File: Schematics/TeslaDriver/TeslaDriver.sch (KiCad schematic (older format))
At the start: 53 parts, among them P1 CONTROL, P2 PWR_IN+, P3 PWR_GND, P4 PWR_OUT_L2, P5 PWR_OUT_L1, Q1 STP65NF06, Q2 STP65NF06, Q3 STP65NF06, Q4 STP65NF06, T1 GateTR10x4, T2 GateTR10x4, T3 GateTR10x4, T4 GateTR10x4, U1 DS18B20, U2 DS18B20, U3 UCC27424D, U4 UCC27424D

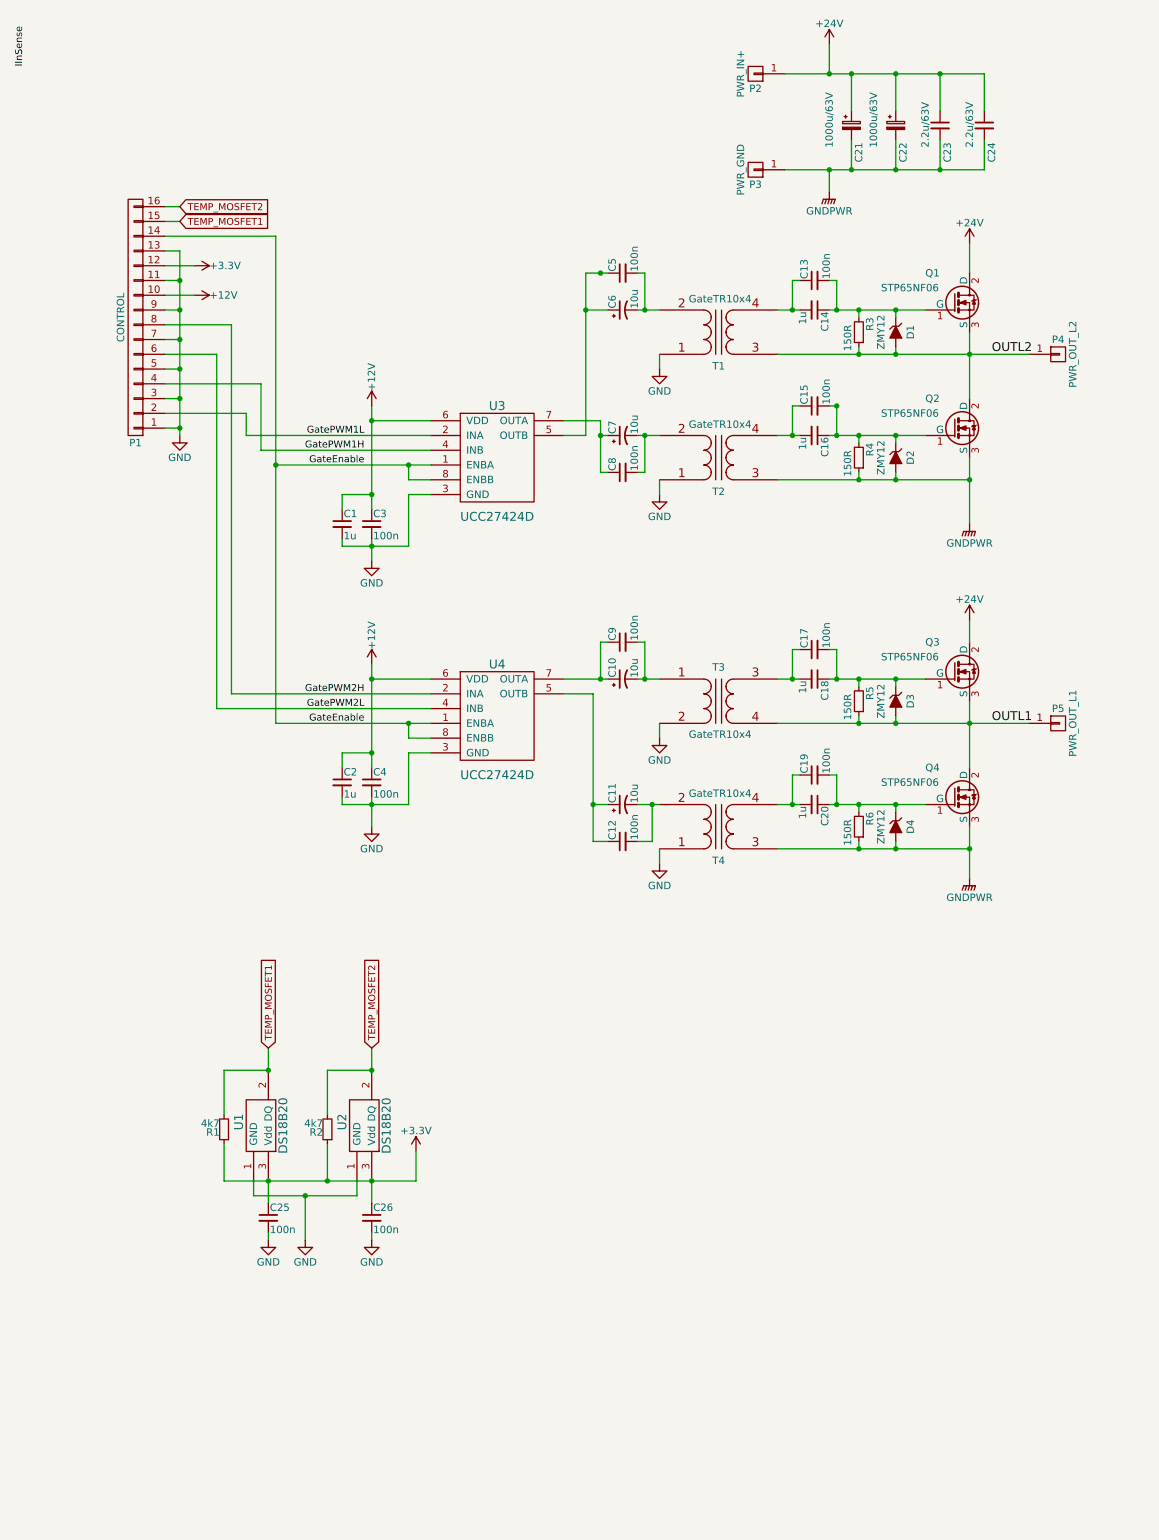
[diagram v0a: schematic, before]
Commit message: * Redesigned the inverter gate driver. 	- It will now drive the gate to ~+-12V rather than ~-0.6 to 11.4. 	- Redesigned the gate clamping to better enforce the gate voltage 	  limit and to more quickly adapt the gate transformers DC level when 	  changing duty cycle.
* Redesigned the inverter PCB.
	- Made an entirely new layout for the inverter PCB which hopefully
	  will be able to carry substantial currents without needing extra
	  bus bars. It should also give parasitic inductances on the board
	  less oportunity to mess with the GS voltage.
	- Designed for manufacturing on a board-hose rather than home
	  etch.
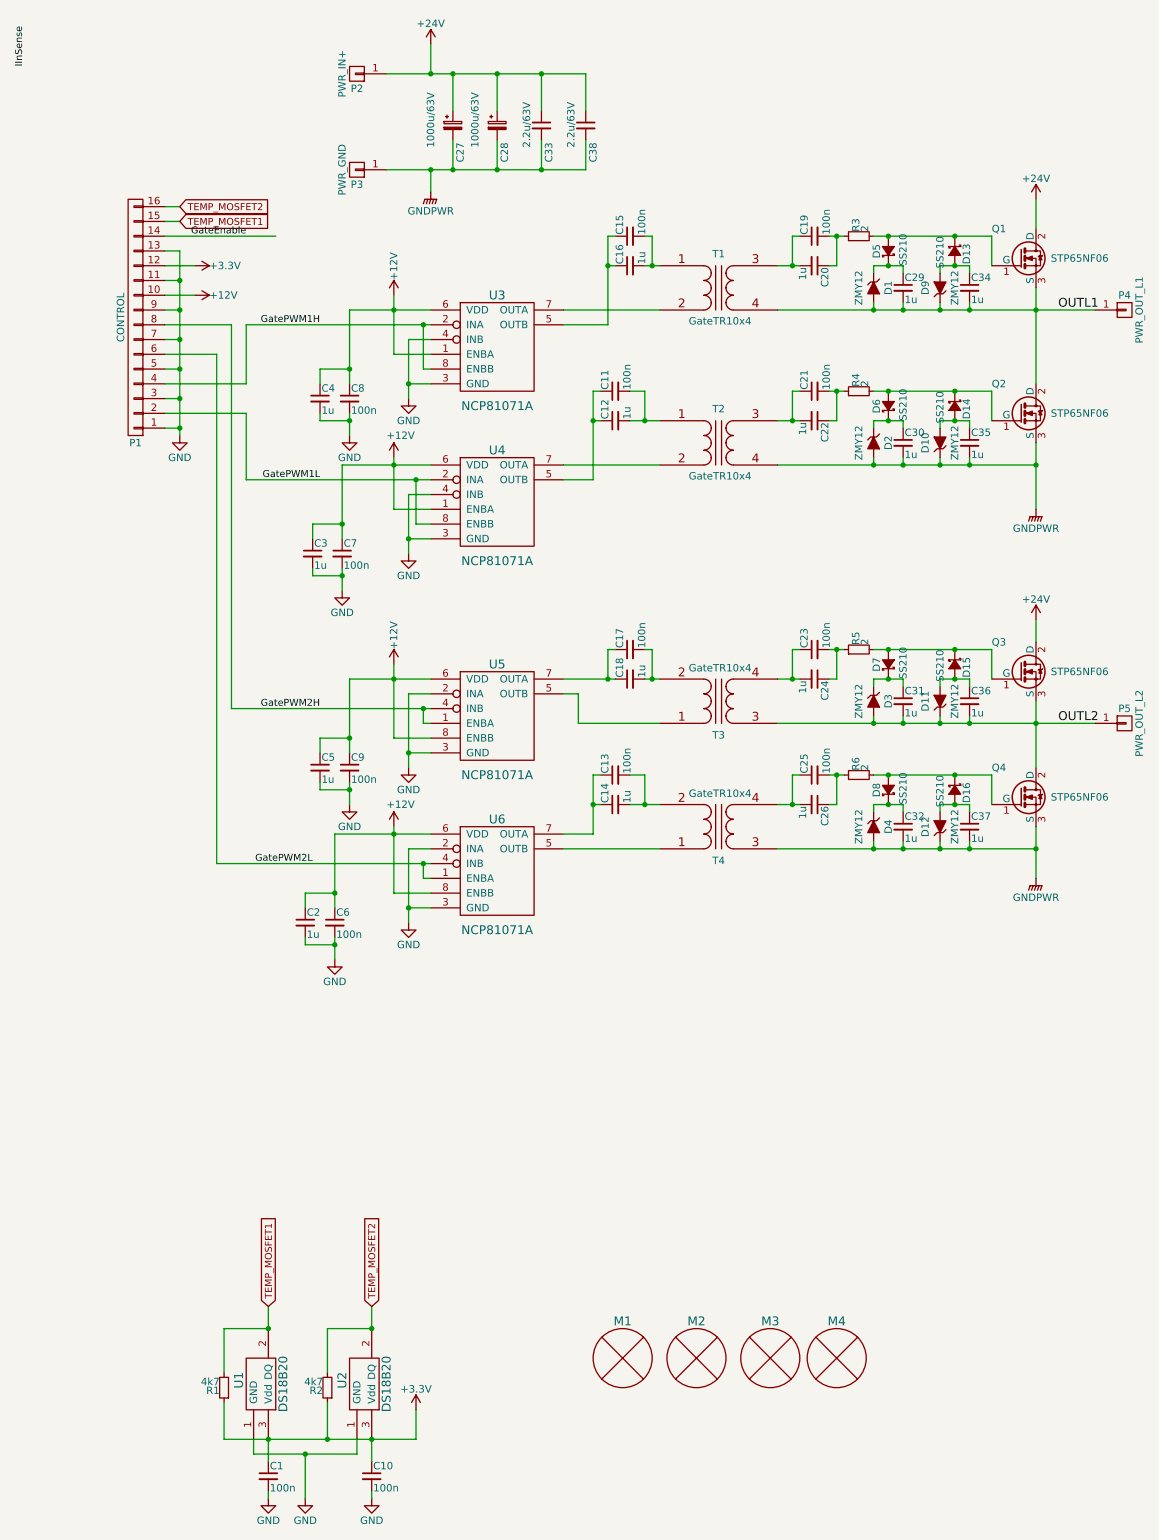
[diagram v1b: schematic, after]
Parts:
- removed C10, C11, C6, C7: 10u, Capacitors_Tantalum_SMD:TantalC_SizeB_EIA-3528_Reflow, symbol CP1_Small
- removed C15, C4, C8: 100n, MyCapacitors:C_0603, symbol C_Small
- removed U3, U4: UCC27424D, MyFootprints:SOIC-8_3.9x4.9mm_Pitch1.27mm, symbol UCC27424D
- added C11, C21, C23, C25, C6, C7: 100n, MyCapacitors:C_0603, symbol C_Small
- added C22, C24, C26: 1u, Capacitors_SMD:C_0603, symbol C_Small
- added C29, C3, C30, C31, C32, C34, C35, C36, C37, C5: 1u, MyCapacitors:C_0603, symbol C_Small
- added D10, D11, D12, D9: ZMY12, MyDiodes:MELF_Standard, symbol ZENERsmall
- added D13, D14, D15, D16, D5, D6, D7, D8: SS210, MyDiodes:Diode-SMA_Standard, symbol SS210
- added M1, M2, M3, M4: MountingHole, MyMechanical:MH7x3, symbol MountingHole
- added U3, U4, U5, U6: NCP81071A, MyFootprints:SOIC-8_3.9x4.9mm_Pitch1.27mm, symbol NCP81071A
- C12: value 100n -> 1u
- C14, C16, C18: footprint Capacitors_SMD:C_0603 -> MyCapacitors:C_0603
- P2, P3: footprint MyConnectors:PowerPad10 -> MyConnectors:PowerPad15_5
- P4: value PWR_OUT_L2 -> PWR_OUT_L1; footprint MyConnectors:PowerPad10 -> MyConnectors:PowerPad15_5
- P5: value PWR_OUT_L1 -> PWR_OUT_L2; footprint MyConnectors:PowerPad10 -> MyConnectors:PowerPad15_5
- R3, R4, R5, R6: value 150R -> 2
- renumbered C25 to C1, C26 to C10, C5 to C15, C21 to C27, C22 to C28, C23 to C33, C24 to C38, C1 to C4, C3 to C8
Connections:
- net +12V: now also C9.1, C3.1, C5.1, C6.1, C7.1, U3.1 (ENBA), U3.6 (VDD), U4.1 (ENBA), U4.6 (VDD), U5.6 (VDD), U5.8 (ENBB), U6.6 (VDD), U6.8 (ENBB)
- net GND: now also C9.2, C3.2, C5.2, C6.2, C7.2, U3.3 (GND), U3.4 (INB), U4.3 (GND), U4.4 (INB), U5.2 (INA), U5.3 (GND), U6.2 (INA), U6.3 (GND); no longer T1.1 (P1), T2.1 (P1), T3.2 (P2), T4.1 (P1)
- net GNDPWR: now also T2.4 (S2), C30.2, C32.2, C35.2, C37.2, D10.1 (K), D12.1 (K); no longer R4.1, R6.1, T2.3 (S1)
- net GatePWM1H: now also U3.2 (INA), U3.8 (ENBB)
- net GatePWM1L: now also U4.2 (INA), U4.8 (ENBB)
- net GatePWM2H: now also U5.1 (ENBA), U5.4 (INB)
- net GatePWM2L: now also U6.1 (ENBA), U6.4 (INB)
- net OUTL1: now also D1.2 (A), P4.1 (P1), Q1.3 (S), Q2.2 (D), T1.4 (S2), C29.2, C34.2, D9.1 (K); no longer D3.2 (A), P5.1 (P1), Q3.3 (S), Q4.2 (D), R5.1, T3.4 (S2)
- net OUTL2: now also D3.2 (A), P5.1 (P1), Q3.3 (S), Q4.2 (D), T3.3 (S1), C31.2, C36.2, D11.1 (K); no longer D1.2 (A), P4.1 (P1), Q1.3 (S), Q2.2 (D), R3.1, T1.3 (S1)
- net at C15.1: now also C16.1, U3.5 (OUTB)
- net at C15.2: now also C16.2, T1.1 (P1); no longer T1.2 (P2)
- net at Q2.1 (G), R4.2: now also D14.1 (K), D6.2 (A); no longer C16.1, D2.1 (K)
- net at T2.2 (P2): now also U4.7 (OUTA)
- net at C12.1: now also C11.1, U4.5 (OUTB)
- net at T3.1 (P1): now also U5.5 (OUTB); no longer C9.2
- net at C12.2: now also T2.1 (P1), C11.2; no longer T4.2 (P2)
- net at C19.1, C20.2: now also T1.3 (S1); no longer T4.4 (S2)
- new net: D13.1 (K), D5.2 (A), Q1.1 (G), R3.2
- new net: T1.2 (P2), U3.7 (OUTA)
- new net: C21.1, C22.2, T2.3 (S1)
- new net: D15.1 (K), D7.2 (A), Q3.1 (G), R5.2
- new net: C17.2, C18.2, T3.2 (P2)
- new net: C23.1, C24.2, T3.4 (S2)
- new net: D16.1 (K), D8.2 (A), Q4.1 (G), R6.2
- new net: T4.1 (P1), U6.5 (OUTB)
- new net: C13.2, C14.2, T4.2 (P2)
- new net: C25.1, C26.2, T4.4 (S2)
- new net: C17.1, C18.1, U5.7 (OUTA)
- new net: C13.1, C14.1, U6.7 (OUTA)
- new net: C32.1, D4.1 (K), D8.1 (K)
- new net: C37.1, D12.2 (A), D16.2 (A)
- new net: C25.2, C26.1, R6.1
- new net: C31.1, D3.1 (K), D7.1 (K)
- new net: C36.1, D11.2 (A), D15.2 (A)
- new net: C23.2, C24.1, R5.1
- new net: C30.1, D2.1 (K), D6.1 (K)
- new net: C35.1, D10.2 (A), D14.2 (A)
- new net: C21.2, C22.1, R4.1
- new net: C29.1, D1.1 (K), D5.1 (K)
- new net: C34.1, D13.2 (A), D9.2 (A)
- new net: C19.2, C20.1, R3.1
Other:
- moved on the sheet: C1, C10, C15, C27, C28, C33, C38, C4, C8, P2, P3, P4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

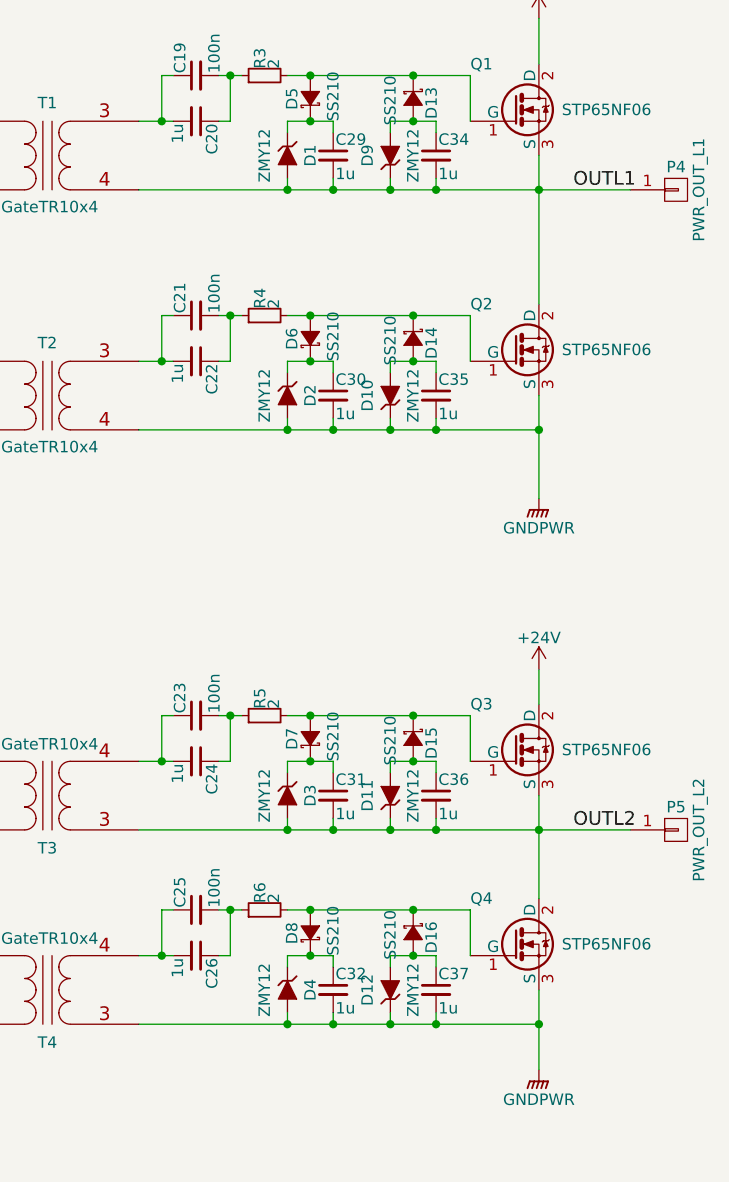
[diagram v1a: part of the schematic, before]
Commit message: Did some small component value tweeks and sorted the BOM.
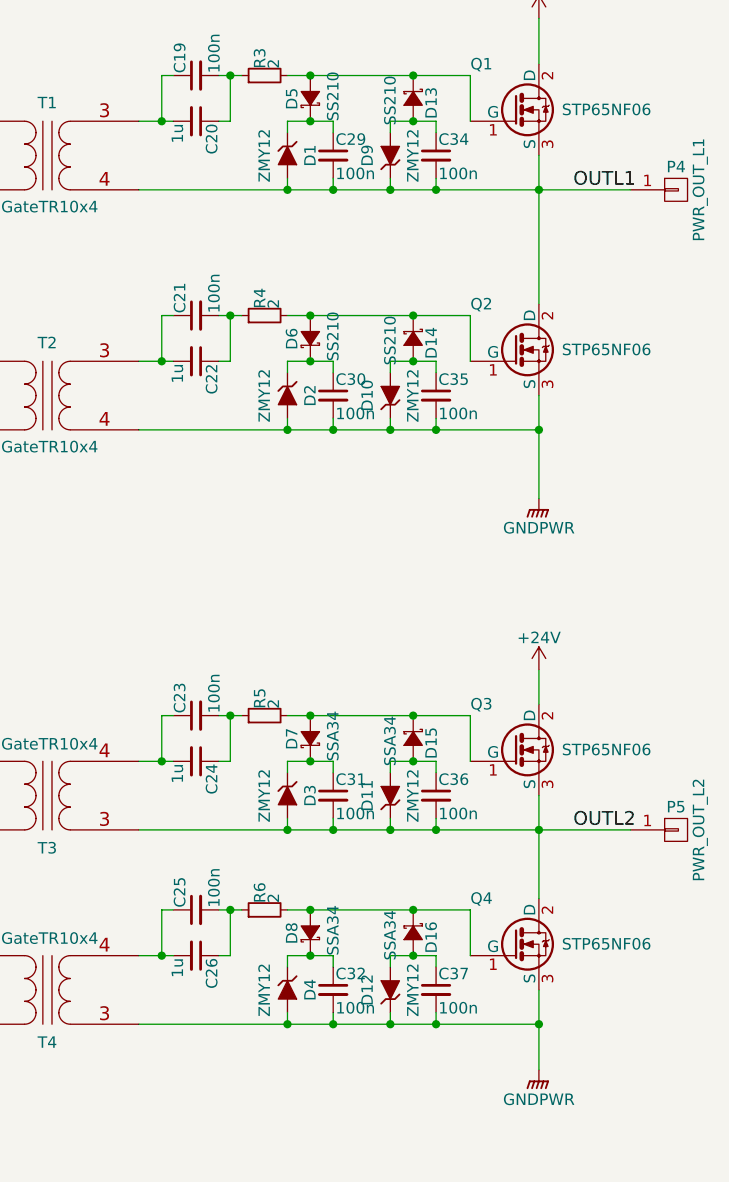
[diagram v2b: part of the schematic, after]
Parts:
- C29, C30, C31, C32, C34, C35, C36, C37: value 1u -> 100n
- D15, D16, D7, D8: value SS210 -> SSA34
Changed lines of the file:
@@
 P 6550 5850
 F 0 "D8" H 6500 5930 50  0000 L CNN
-F 1 "SS210" H 6450 5750 50  0000 L CNN
+F 1 "SSA34" H 6450 5750 50  0000 L CNN
 F 2 "MyDiodes:Diode-SMA_Standard" V 6550 5850 60  0001 C CNN
 F 3 "" V 6550 5850 60  0000 C CNN
@@
 P 6650 6100
 F 0 "C32" H 6660 6170 50  0000 L CNN
-F 1 "1u" H 6660 6020 50  0000 L CNN
+F 1 "100n" H 6660 6020 50  0000 L CNN
 F 2 "MyCapacitors:C_0603" H 6650 6100 60  0001 C CNN
 F 3 "" H 6650 6100 60  0000 C CNN
@@
 P 7100 6100
 F 0 "C37" H 7110 6170 50  0000 L CNN
-F 1 "1u" H 7110 6020 50  0000 L CNN
+F 1 "100n" H 7110 6020 50  0000 L CNN
 F 2 "MyCapacitors:C_0603" H 7100 6100 60  0001 C CNN
 F 3 "" H 7100 6100 60  0000 C CNN
@@
 P 7000 5850
 F 0 "D16" H 6950 5930 50  0000 L CNN
-F 1 "SS210" H 6900 5750 50  0000 L CNN
+F 1 "SSA34" H 6900 5750 50  0000 L CNN
 F 2 "MyDiodes:Diode-SMA_Standard" V 7000 5850 60  0001 C CNN
 F 3 "" V 7000 5850 60  0000 C CNN
@@
 P 6550 5000
 F 0 "D7" H 6500 5080 50  0000 L CNN
-F 1 "SS210" H 6450 4900 50  0000 L CNN
+F 1 "SSA34" H 6450 4900 50  0000 L CNN
 F 2 "MyDiodes:Diode-SMA_Standard" V 6550 5000 60  0001 C CNN
 F 3 "" V 6550 5000 60  0000 C CNN
@@
 P 6650 5250
 F 0 "C31" H 6660 5320 50  0000 L CNN
-F 1 "1u" H 6660 5170 50  0000 L CNN
+F 1 "100n" H 6660 5170 50  0000 L CNN
 F 2 "MyCapacitors:C_0603" H 6650 5250 60  0001 C CNN
 F 3 "" H 6650 5250 60  0000 C CNN
@@
 P 7100 5250
 F 0 "C36" H 7110 5320 50  0000 L CNN
-F 1 "1u" H 7110 5170 50  0000 L CNN
+F 1 "100n" H 7110 5170 50  0000 L CNN
 F 2 "MyCapacitors:C_0603" H 7100 5250 60  0001 C CNN
 F 3 "" H 7100 5250 60  0000 C CNN
@@
 P 7000 5000
 F 0 "D15" H 6950 5080 50  0000 L CNN
-F 1 "SS210" H 6900 4900 50  0000 L CNN
+F 1 "SSA34" H 6900 4900 50  0000 L CNN
 F 2 "MyDiodes:Diode-SMA_Standard" V 7000 5000 60  0001 C CNN
 F 3 "" V 7000 5000 60  0000 C CNN
@@
 P 6650 3500
 F 0 "C30" H 6660 3570 50  0000 L CNN
-F 1 "1u" H 6660 3420 50  0000 L CNN
+F 1 "100n" H 6660 3420 50  0000 L CNN
 F 2 "MyCapacitors:C_0603" H 6650 3500 60  0001 C CNN
 F 3 "" H 6650 3500 60  0000 C CNN
@@
 P 7100 3500
 F 0 "C35" H 7110 3570 50  0000 L CNN
-F 1 "1u" H 7110 3420 50  0000 L CNN
+F 1 "100n" H 7110 3420 50  0000 L CNN
 F 2 "MyCapacitors:C_0603" H 7100 3500 60  0001 C CNN
 F 3 "" H 7100 3500 60  0000 C CNN
@@
 P 6650 2450
 F 0 "C29" H 6660 2520 50  0000 L CNN
-F 1 "1u" H 6660 2370 50  0000 L CNN
+F 1 "100n" H 6660 2370 50  0000 L CNN
 F 2 "MyCapacitors:C_0603" H 6650 2450 60  0001 C CNN
 F 3 "" H 6650 2450 60  0000 C CNN
@@
 P 7100 2450
 F 0 "C34" H 7110 2520 50  0000 L CNN
-F 1 "1u" H 7110 2370 50  0000 L CNN
+F 1 "100n" H 7110 2370 50  0000 L CNN
 F 2 "MyCapacitors:C_0603" H 7100 2450 60  0001 C CNN
 F 3 "" H 7100 2450 60  0000 C CNN
